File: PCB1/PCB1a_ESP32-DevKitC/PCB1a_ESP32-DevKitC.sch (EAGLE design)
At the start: 40 parts, among them J1 691357310006B, J2 618009231421, J3 ESP32_DEVC_MIN_LEFT, J4 ESP32_DEVC_MIN_RIGHT, U2 MAX232D, U4 TLE9250VSJ, U8 74AHCT245, U9 74AHCT245

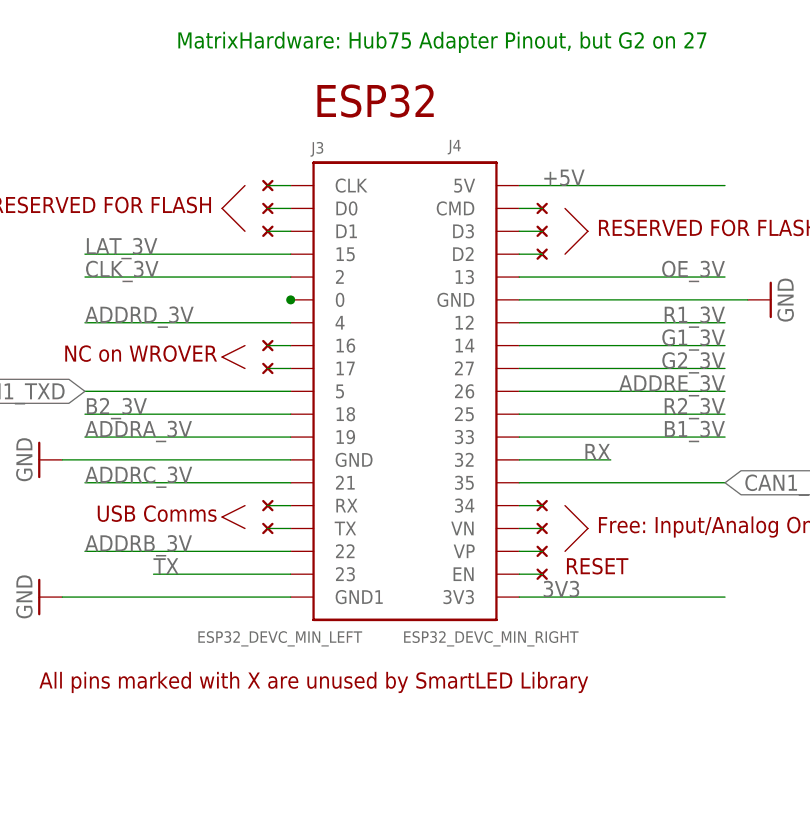
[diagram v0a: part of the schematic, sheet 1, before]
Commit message: SMD Connectors.
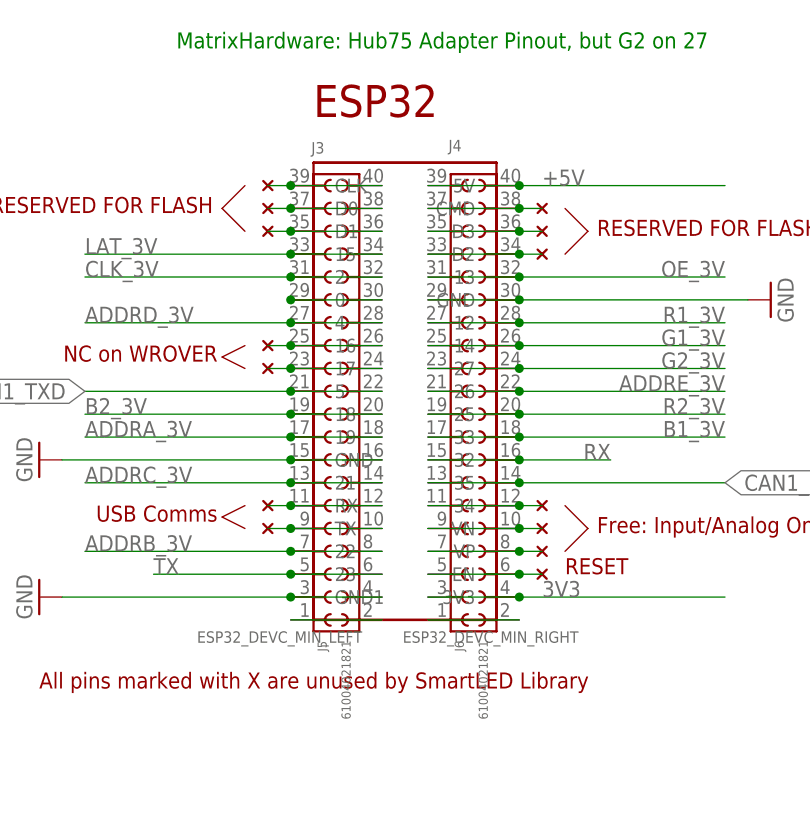
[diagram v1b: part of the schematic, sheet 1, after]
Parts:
- added J5, J6: 61004021821, Wurth_Connectors_WR-PHD:6100XX21821_61004021821
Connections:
- new net N$12: J5.1, J5.2
- new net N$18: J6.1, J6.2
- new net N$4: J3.GND1, J5.3, J5.4
- net +5V: now also J6.39, J6.40
- net 3V3: now also J6.3, J6.4
- net ADDRA_3V: now also J5.17, J5.18
- net ADDRB_3V: now also J5.7, J5.8
- net ADDRC_3V: now also J5.13, J5.14
- net ADDRD_3V: now also J5.27, J5.28
- net ADDRE_3V: now also J6.21, J6.22
- net B1_3V: now also J6.17, J6.18
- net B2_3V: now also J5.19, J5.20
- net CAN1_RXD: now also J6.13, J6.14
- net CAN1_TXD: now also J5.21, J5.22
- net CLK_3V: now also J5.31, J5.32
- net G1_3V: now also J6.25, J6.26
- net G2_3V: now also J6.23, J6.24
- net GND: now also J5.15, J5.16, J6.29, J6.30; no longer J3.GND1
- net LAT_3V: now also J5.33, J5.34
- net N$1: now also J5.29, J5.30
- net N$10: now also J6.7, J6.8
- net N$11: now also J6.11, J6.12
- net N$13: now also J6.5, J6.6
- net N$14: now also J5.10, J5.9
- net N$15: now also J5.11, J5.12
- net N$16: now also J5.23, J5.24
- net N$17: now also J5.25, J5.26
- net N$2: now also J6.37, J6.38
- net N$3: now also J6.35, J6.36
- net N$5: now also J6.33, J6.34
- net N$6: now also J5.39, J5.40
- net N$7: now also J5.37, J5.38
- net N$8: now also J5.35, J5.36
- net N$9: now also J6.10, J6.9
- net OE_3V: now also J6.31, J6.32
- net R1_3V: now also J6.27, J6.28
- net R2_3V: now also J6.19, J6.20
- net RX: now also J6.15, J6.16
- net TX: now also J5.5, J5.6

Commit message: rm THT
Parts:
- removed J3: ESP32_DEVC_MIN_LEFT, eclibrary:ESP32_DEVC_MIN_LEFT
- removed J4: ESP32_DEVC_MIN_RIGHT, eclibrary:ESP32_DEVC_MIN_RIGHT
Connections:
- net +5V: no longer J4.5V
- net 3V3: no longer J4.3V3
- net ADDRA_3V: no longer J3.19
- net ADDRB_3V: no longer J3.22
- net ADDRC_3V: no longer J3.21
- net ADDRD_3V: no longer J3.4
- net ADDRE_3V: no longer J4.26
- net B1_3V: no longer J4.33
- net B2_3V: no longer J3.18
- net CAN1_RXD: no longer J4.35
- net CAN1_TXD: no longer J3.5
- net CLK_3V: no longer J3.2
- net G1_3V: no longer J4.14
- net G2_3V: no longer J4.27
- net GND: no longer J3.GND, J4.GND
- net LAT_3V: no longer J3.15
- net N$1: no longer J3.0
- net N$10: no longer J4.VP
- net N$11: no longer J4.34
- net N$13: no longer J4.EN
- net N$14: no longer J3.TX
- net N$15: no longer J3.RX
- net N$16: no longer J3.17
- net N$17: no longer J3.16
- net N$2: no longer J4.CMD
- net N$3: no longer J4.D3
- net N$4: no longer J3.GND1
- net N$5: no longer J4.D2
- net N$6: no longer J3.CLK
- net N$7: no longer J3.D0
- net N$8: no longer J3.D1
- net N$9: no longer J4.VN
- net OE_3V: no longer J4.13
- net R1_3V: no longer J4.12
- net R2_3V: no longer J4.25
- net RX: no longer J4.32
- net TX: no longer J3.23

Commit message: ..
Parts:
- added C2, C5: 100nF, Wurth_Capacitors_WCAP-CSGP:WCAP-CSGP_0805_H0.8_885012207098_50V(DC)_R
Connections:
- removed net 3V3: J6.3, J6.4
- removed net VCC: C3.1, C4.2, U2.VCC
- net +3V3: now also C3.1, C4.2, J6.3, J6.4, U2.VCC
- net +5V: now also C2.2, C5.2
- net GND: now also C2.1, C5.1

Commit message: thermals="no"/>
thermals="no"/>
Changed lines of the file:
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@@
 </plain>
 <instances>
-<instance part="GND1" gate="1" x="116.84" y="104.14" smashed="yes">
-<attribute name="VALUE" x="114.3" y="101.6" size="1.778" layer="96"/>
+<instance part="GND1" gate="1" x="132.08" y="111.76" smashed="yes">
+<attribute name="VALUE" x="129.54" y="109.22" size="1.778" layer="96"/>
 </instance>
 <instance part="HUB75RGB" gate="G$1" x="95.25" y="71.12" smashed="yes" rot="R270">

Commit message: Go Production
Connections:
- net N$1 renamed 0
- net N$10 renamed VP
- net N$11 renamed 34
- net N$13 renamed EN
- net N$14 renamed USB_TX
- net N$15 renamed USB_RX
- net N$16 renamed 17
- net N$17 renamed 16
- net N$2 renamed CMD
- net N$3 renamed D3
- net N$5 renamed D2
- net N$6 renamed CLK
- net N$7 renamed D0
- net N$8 renamed D1
- net N$9 renamed VN
- removed net B2_3V: J5.19, J5.20, U9.A6
- removed net G2_3V: J6.23, J6.24, U9.A4
- removed net M1_B2: HUB75RGB..7, HUB75RGB.7, U9.B6
- removed net M1_G2: HUB08RG.12, HUB75RGB..6, HUB75RGB.6, U9.B4
- removed net M1_R2: HUB08RG.11, HUB75RGB..5, HUB75RGB.5, U9.B5
- removed net N$12: J5.1, J5.2
- removed net N$18: J6.1, J6.2
- removed net N$4: J5.3, J5.4
- removed net R2_3V: J6.19, J6.20, U9.A5
- new net B0_3V: J6.17, J6.18, U9.A3
- new net G0_3V: J6.25, J6.26, U9.A2
- new net M1_B0: HUB75RGB..3, HUB75RGB.3, U9.B3
- new net M1_G0: HUB08RG.10, HUB12RG.14, HUB75RGB..2, HUB75RGB.2, U9.B2
- new net M1_R0: HUB08RG.9, HUB12RG.12, HUB75RGB..1, HUB75RGB.1, U9.B1
- new net R0_3V: J6.27, J6.28, U9.A1
- net B1_3V: now also J5.19, J5.20, U9.A6; no longer J6.17, J6.18, U9.A3
- net G1_3V: now also J6.23, J6.24, U9.A4; no longer J6.25, J6.26, U9.A2
- net GND: now also J5.1, J5.2, J5.3, J5.4, J6.1, J6.2
- net M1_B1: now also HUB75RGB..7, HUB75RGB.7, U9.B6; no longer HUB75RGB..3, HUB75RGB.3, U9.B3
- net M1_G1: now also HUB08RG.12, HUB75RGB..6, HUB75RGB.6, U9.B4; no longer HUB08RG.10, HUB12RG.14, HUB75RGB..2, HUB75RGB.2, U9.B2
- net M1_R1: now also HUB08RG.11, HUB75RGB..5, HUB75RGB.5, U9.B5; no longer HUB08RG.9, HUB12RG.12, HUB75RGB..1, HUB75RGB.1, U9.B1
- net R1_3V: now also J6.19, J6.20, U9.A5; no longer J6.27, J6.28, U9.A1
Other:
- moved on the sheet: J5, J6
